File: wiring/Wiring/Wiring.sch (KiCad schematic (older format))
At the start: 4 parts

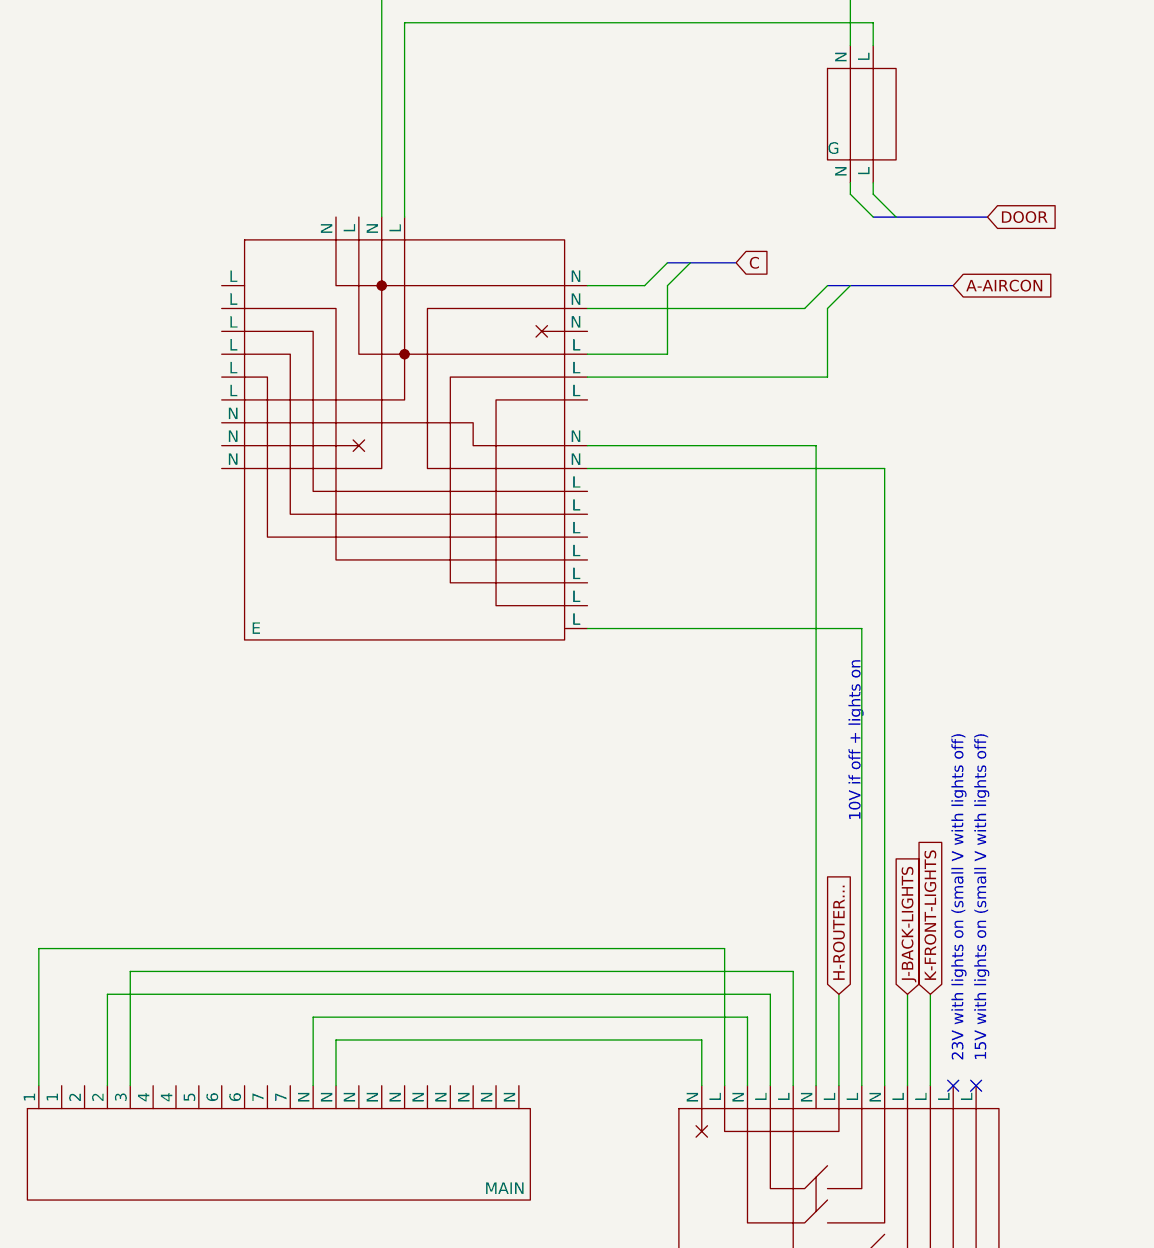
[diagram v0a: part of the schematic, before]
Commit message: Fix wrong wiring
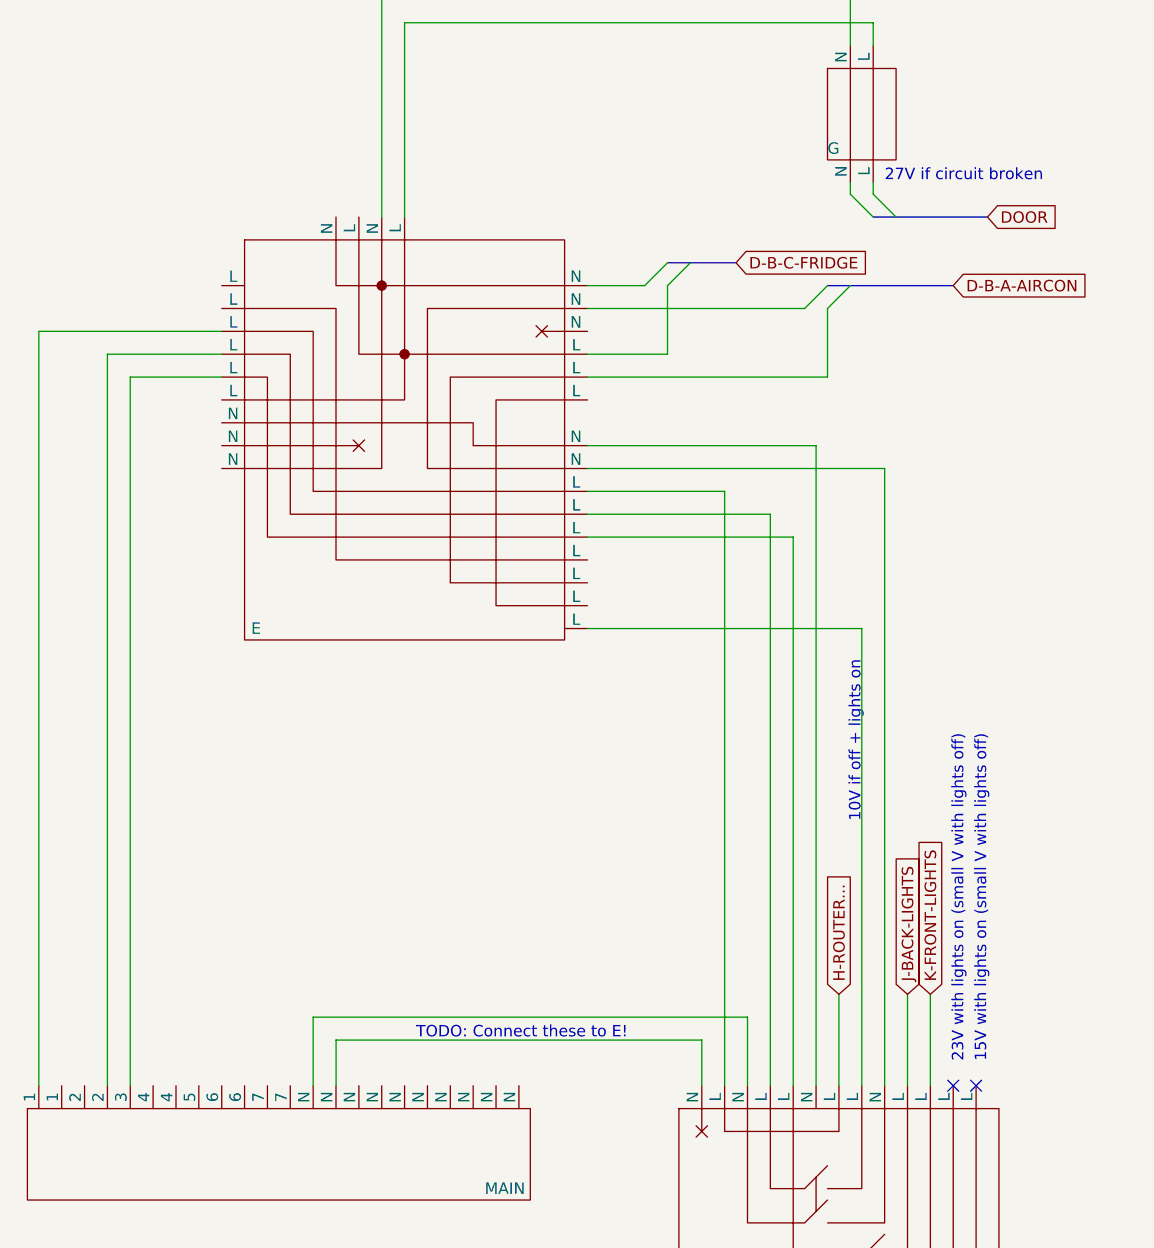
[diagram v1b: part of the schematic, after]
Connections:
- net at U?.2 (L): now also U?.18 (L); no longer U?.1
- net at U?.4 (L): now also U?.19 (L); no longer U?.2
- net at U?.5 (L): now also U?.20 (L); no longer U?.3
- net at U?.5 (L): now also U?.3
- net at U?.6 (L): now also U?.2
- net at U?.7 (L): now also U?.1
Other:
- note added: "27V if circuit broken"
- note added: "TODO: Connect these to E!"
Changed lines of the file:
@@
 	1    0    0    -1
 $EndComp
-Wire Wire Line
-	3900 5400 3900 5000
-Wire Wire Line
-	6800 5000 6800 5400
 Entry Wire Line
 	6950 2000 7050 1900
@@
 	7150 1900 7050 2000
 Text GLabel 7600 1900 2    50   Input ~ 0
-A-AIRCON
+D-B-A-AIRCON
 Entry Wire Line
 	7250 1500 7350 1600
@@
 	6350 2200 6000 2200
 Text GLabel 6650 1800 2    50   Input ~ 0
-C
+D-B-C-FRIDGE
 Wire Wire Line
 	7100 5000 7100 5400
 Text GLabel 7100 5000 1    50   Input ~ 0
 H-ROUTER...
-Wire Wire Line
-	6600 5400 6600 4800
-Wire Wire Line
-	6600 4800 3600 4800
-Wire Wire Line
-	3600 4800 3600 5400
 Text GLabel 7400 5000 1    50   Input ~ 0
 J-BACK-LIGHTS
@@
 	4900 5200 4900 5400
 Wire Wire Line
-	4000 5400 4000 4900
-Wire Wire Line
-	4000 4900 6900 4900
-Wire Wire Line
-	6900 4900 6900 5400
-Wire Wire Line
 	7500 5400 7500 5000
 Text GLabel 7500 5000 1    50   Input ~ 0
@@
 	4800 5100 4800 5400
 Wire Wire Line
-	6800 5000 3900 5000
+	3600 2100 4400 2100
+Wire Wire Line
+	3900 2200 4400 2200
+Wire Wire Line
+	4000 2300 4400 2300
+Wire Wire Line
+	6600 2800 6000 2800
+Wire Wire Line
+	6600 2800 6600 5400
+Wire Wire Line
+	3600 2100 3600 5400
+Wire Wire Line
+	6000 2900 6800 2900
+Wire Wire Line
+	6800 2900 6800 5400
+Wire Wire Line
+	3900 2200 3900 5400
+Wire Wire Line
+	6000 3000 6900 3000
 Wire Bus Line
 	6350 1800 6650 1800
@@
 Wire Bus Line
 	7050 1900 7600 1900
+Wire Wire Line
+	4000 2300 4000 5400
+Wire Wire Line
+	6900 3000 6900 5400
+Text Notes 5250 5200 0    50   ~ 0
+TODO: Connect these to E!
+Text Notes 7300 1450 0    50   ~ 0
+27V if circuit broken
 $EndSCHEMATC

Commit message: Add layout
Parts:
- U1, U2, U3, U4: renamed from U?; footprint (none) -> Package_DFN_QFN:DFN-8-1EP_4x4mm_P0.8mm_EP2.5x3.6mm
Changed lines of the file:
@@
 $EndDescr
 $Comp
-L Wiring:F U?
+L Wiring:F U3
 U 1 1 5ED38158
 P 7050 5850
-F 0 "U?" H 7678 5929 50  0001 L CNN
+F 0 "U3" H 7678 5929 50  0001 L CNN
 F 1 "F" H 7650 5450 50  0000 L CNN
-F 2 "" H 7000 6000 50  0001 C CNN
+F 2 "Package_DFN_QFN:DFN-8-1EP_4x4mm_P0.8mm_EP2.5x3.6mm" H 7000 6000 50  0001 C CNN
 F 3 "" H 7000 6000 50  0001 C CNN
 	1    7050 5850
@@
 $EndComp
 $Comp
-L Wiring:E U?
+L Wiring:E U2
 U 1 1 5ED38C33
 P 5200 2550
-F 0 "U?" H 4525 3500 50  0001 C CNN
+F 0 "U2" H 4525 3500 50  0001 C CNN
 F 1 "E" H 4550 1700 50  0000 C CNN
-F 2 "" H 5200 2550 50  0001 C CNN
+F 2 "Package_DFN_QFN:DFN-8-1EP_4x4mm_P0.8mm_EP2.5x3.6mm" H 5200 2550 50  0001 C CNN
 F 3 "" H 5200 2550 50  0001 C CNN
 	1    5200 2550
@@
 $EndComp
 $Comp
-L Wiring:G U?
+L Wiring:G U4
 U 1 1 5ED3C88F
 P 7200 1150
-F 0 "U?" H 7378 1196 50  0001 L CNN
+F 0 "U4" H 7378 1196 50  0001 L CNN
 F 1 "G" H 7050 1000 50  0000 L CNN
-F 2 "" H 7200 1150 50  0001 C CNN
+F 2 "Package_DFN_QFN:DFN-8-1EP_4x4mm_P0.8mm_EP2.5x3.6mm" H 7200 1150 50  0001 C CNN
 F 3 "" H 7200 1150 50  0001 C CNN
 	1    7200 1150
@@
 	7250 750  7250 850
 $Comp
-L Wiring:MAIN U?
+L Wiring:MAIN U1
 U 1 1 5ED3FA8D
 P 4650 5700
-F 0 "U?" H 3600 5850 50  0001 L CNN
+F 0 "U1" H 3600 5850 50  0001 L CNN
 F 1 "MAIN" H 5550 5550 50  0000 L CNN
-F 2 "" H 4650 6000 50  0001 C CNN
+F 2 "Package_DFN_QFN:DFN-8-1EP_4x4mm_P0.8mm_EP2.5x3.6mm" H 4650 6000 50  0001 C CNN
 F 3 "" H 4650 6000 50  0001 C CNN
 	1    4650 5700

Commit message: Add rough outlines of boxes H, I, J
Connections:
- net H-ROUTER...: no longer names the net of U3.7 (L)
- net J-BACK-LIGHTS: no longer names the net of U3.10 (L)
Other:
- note added: "H"
- note added: "I"
- note added: "J"
- note added: "L"
- note added: "N"
- note added: "Route these through E\n(can't be connected \nstraight to H)"
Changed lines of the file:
@@
 D-B-C-FRIDGE
-Wire Wire Line
-	7100 5000 7100 5400
-Text GLabel 7100 5000 1    50   Input ~ 0
-H-ROUTER...
-Text GLabel 7400 5000 1    50   Input ~ 0
-J-BACK-LIGHTS
-Wire Wire Line
-	7400 5000 7400 5400
 Wire Wire Line
 	6700 5400 6700 5100
@@
 Wire Wire Line
 	6000 3000 6900 3000
-Wire Bus Line
-	6350 1800 6650 1800
-Wire Bus Line
-	7250 1600 7750 1600
-Wire Bus Line
-	7050 1900 7600 1900
 Wire Wire Line
 	4000 2300 4000 5400
@@
 Text Notes 7300 1450 0    50   ~ 0
 27V if circuit broken
+Wire Notes Line
+	9000 2500 9500 2500
+Wire Notes Line
+	9500 2500 9500 3100
+Wire Notes Line
+	9000 3100 9000 2500
+Text Notes 9400 3050 0    50   ~ 0
+H
+Wire Notes Line
+	10500 2500 11000 2500
+Wire Notes Line
+	11000 2500 11000 3100
+Wire Notes Line
+	11000 3100 10500 3100
+Wire Notes Line
+	10500 3100 10500 2500
+Text Notes 10950 3050 0    50   ~ 0
+J
+Wire Wire Line
+	7100 2600 7100 5400
+Text GLabel 11750 2500 2    50   Input ~ 0
+Router
+Entry Wire Line
+	11300 2600 11400 2500
+Wire Wire Line
+	11300 2600 7100 2600
+Wire Wire Line
+	5000 5400 5000 5300
+Wire Wire Line
+	5000 5300 6100 5300
+Wire Wire Line
+	6100 5300 6100 6450
+Wire Wire Line
+	6100 6450 8750 6450
+Wire Wire Line
+	8750 6450 8750 2750
+Entry Wire Line
+	11550 2500 11450 2600
+Wire Wire Line
+	11450 2700 11450 2600
+Wire Notes Line
+	8500 3500 9000 3500
+Wire Notes Line
+	9000 3500 9000 4000
+Wire Notes Line
+	9000 4000 8500 4000
+Wire Notes Line
+	8500 4000 8500 3500
+Text Notes 8950 3950 0    50   ~ 0
+I
+Wire Wire Line
+	7400 2900 11300 2900
+Wire Wire Line
+	7400 2900 7400 5400
+Wire Notes Line
+	9500 3100 9000 3100
+Text Notes 7650 2850 0    50   ~ 0
+Route these through E\n(can't be connected \nstraight to H)
+Wire Wire Line
+	10750 2700 11450 2700
+Wire Wire Line
+	10750 2750 10750 2700
+Wire Wire Line
+	8750 2750 10750 2750
+Wire Wire Line
+	10750 2750 10750 2800
+Wire Wire Line
+	10750 2800 11450 2800
+Connection ~ 10750 2750
+Text Notes 11000 2600 0    50   ~ 0
+L
+Text Notes 11000 2700 0    50   ~ 0
+N
+Text Notes 11000 2800 0    50   ~ 0
+N
+Text Notes 11000 2900 0    50   ~ 0
+L
+Text Notes 10450 2600 0    50   ~ 0
+L
+Text Notes 10450 2750 0    50   ~ 0
+N
+Text Notes 10450 2900 0    50   ~ 0
+L
+Text Notes 9500 2600 0    50   ~ 0
+L
+Text Notes 9500 2900 0    50   ~ 0
+L
+Text Notes 9500 2750 0    50   ~ 0
+N
+Text Notes 8950 2750 0    50   ~ 0
+N
+Text Notes 8950 2600 0    50   ~ 0
+L
+Text Notes 8950 2900 0    50   ~ 0
+L
+Text Notes 8750 3500 0    50   ~ 0
+N
+Text Notes 8750 4100 0    50   ~ 0
+N
+Text GLabel 11750 3000 2    50   Input ~ 0
+BACK-LIGHTS
+Entry Wire Line
+	11300 2900 11400 3000
+Entry Wire Line
+	11450 2900 11550 3000
+Wire Wire Line
+	11450 2800 11450 2900
+Wire Bus Line
+	11400 3000 11750 3000
+Wire Bus Line
+	11400 2500 11750 2500
+Wire Bus Line
+	6350 1800 6650 1800
+Wire Bus Line
+	7250 1600 7750 1600
+Wire Bus Line
+	7050 1900 7600 1900
 $EndSCHEMATC

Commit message: Connect soldering area, fix routing (incomplete)
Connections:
- net at U3.1 (N): now also U2.16 (N); no longer U1.~ (N)
- net at U3.10 (L): now also U2.19 (L)
- net at U3.4 (L): now also U1.~ (N); no longer U2.19 (L)
- net at U3.6 (N): no longer U2.16 (N)
- net at U3.7 (L): now also U2.23 (L)
- net at U2.1 (N): now also U1.~ (N)
- net at U2.2 (N): now also U1.~ (N)
- net at U2.3 (N): now also U1.~ (N)
- net at U2.4 (L): now also U1.~ (N)
- net at U2.6 (L): no longer U1.2
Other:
- note added: "Q"
- note added: "Route more\nwires through\nI! (WIP comp.)"
- note removed: "Route these through E\n(can't be connected \nstraight to H)"
- note removed: "TODO: Connect these to E!"

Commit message: Add B
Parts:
- added U?: B, symbol Wiring:B
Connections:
- net at U2.10 (N): now also U?.10 (N)
- net at U2.11 (N): now also U?.10 (N)
- net at U2.13 (L): now also U?.12 (L)
- net at U2.14 (L): now also U?.12 (L)
- no-connect marks 2 -> 3
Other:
- note added: "D"

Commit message: Add D
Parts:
- added U?: D, symbol Wiring:D
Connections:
- net at U2.10 (N): now also U?.10 (N); no longer U?.10 (N)
- net at U2.11 (N): now also U?.10 (N); no longer U?.10 (N)
- net at U2.13 (L): now also U?.12 (L); no longer U?.12 (L)
- net at U2.14 (L): now also U?.12 (L)
- net at U?.12 (L): now also U?.9 (L); no longer U2.14 (L)
- net at U?.10 (N): now also U?.8 (N)
- new net: U?.10 (N), U?.8 (N) (x2)
- new net: U?.12 (L), U?.9 (L) (x2)
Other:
- note removed: "D"
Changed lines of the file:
@@
 Entry Wire Line
 	12000 700  11900 800
-Wire Wire Line
-	13400 5200 11500 5200
 Text GLabel 12200 700  2    50   Input ~ 0
 C-FRIDGE...
@@
 Wire Wire Line
 	12800 5700 12800 8400
-Wire Wire Line
-	11500 5300 13200 5300
 Wire Wire Line
 	13000 8400 13000 8000
@@
 Wire Wire Line
 	16950 5800 16950 5900
-$Comp
-L Wiring:E U2
-U 1 1 5ED38C33
-P 10700 5550
-F 0 "U2" H 10025 6500 50  0001 C CNN
-F 1 "E" H 10050 4700 50  0000 C CNN
-F 2 "Package_DFN_QFN:DFN-8-1EP_4x4mm_P0.8mm_EP2.5x3.6mm" H 10700 5550 50  0001 C CNN
-F 3 "" H 10700 5550 50  0001 C CNN
-	1    10700 5550
-	1    0    0    -1
-$EndComp
 Wire Wire Line
 	12300 8400 12300 8000
@@
 Wire Wire Line
 	10950 3650 10600 3650
-Wire Notes Line
-	13000 3500 13500 3500
-Wire Notes Line
-	13500 3500 13500 4000
-Wire Notes Line
-	13500 4000 13000 4000
-Wire Notes Line
-	13000 4000 13000 3500
-Text Notes 13450 4000 0    50   ~ 0
-D
 Wire Wire Line
 	11500 1950 11600 1950
@@
 	11400 1950 11300 1850
 Wire Wire Line
-	13100 5000 13100 1800
-Wire Wire Line
-	13100 1800 12800 1800
-Wire Wire Line
-	11500 5000 13100 5000
-Wire Wire Line
-	13200 1700 12800 1700
-Wire Wire Line
-	13200 1700 13200 5300
-Wire Wire Line
 	11900 800  11900 1100
 Wire Wire Line
 	11800 1100 11800 800
-Wire Wire Line
-	13300 4900 13300 1600
-Wire Wire Line
-	13300 1600 12800 1600
-Wire Wire Line
-	11500 4900 13300 4900
-Wire Wire Line
-	12800 1500 13400 1500
-Wire Wire Line
-	13400 1500 13400 5200
+$Comp
+L Wiring:D U?
+U 1 1 5EE0B04E
+P 14200 1550
+F 0 "U?" H 13650 2050 50  0001 C CNN
+F 1 "D" H 14728 1467 50  0000 L CNN
+F 2 "" H 13500 2050 50  0001 C CNN
+F 3 "" H 13500 2050 50  0001 C CNN
+	1    14200 1550
+	1    0    0    -1
+$EndComp
+Wire Wire Line
+	13950 2150 13950 5000
+Wire Wire Line
+	11500 5000 13950 5000
+Wire Wire Line
+	12800 1800 13600 1800
+Wire Wire Line
+	14050 2150 14050 5300
+Wire Wire Line
+	12800 1700 13600 1700
+Wire Wire Line
+	11500 5300 14050 5300
+Wire Wire Line
+	14150 2150 14150 4900
+Wire Wire Line
+	11500 4900 14150 4900
+Wire Wire Line
+	12800 1600 13600 1600
+Wire Wire Line
+	14250 2150 14250 5200
+Wire Wire Line
+	12800 1500 13600 1500
+Wire Wire Line
+	11500 5200 14250 5200
+Wire Wire Line
+	12800 1300 13600 1300
+Wire Wire Line
+	12800 1400 13600 1400
 Wire Bus Line
 	10850 1850 11400 1850
 Wire Bus Line
+	12600 900  12850 900
+Wire Bus Line
 	11600 2950 11900 2950
 Wire Bus Line
@@
 Wire Bus Line
 	11050 4600 11550 4600
-Wire Bus Line
-	12600 900  12850 900
+$Comp
+L Wiring:E U2
+U 1 1 5ED38C33
+P 10700 5550
+F 0 "U2" H 10025 6500 50  0001 C CNN
+F 1 "E" H 10050 4700 50  0000 C CNN
+F 2 "Package_DFN_QFN:DFN-8-1EP_4x4mm_P0.8mm_EP2.5x3.6mm" H 10700 5550 50  0001 C CNN
+F 3 "" H 10700 5550 50  0001 C CNN
+	1    10700 5550
+	1    0    0    -1
+$EndComp
 $EndSCHEMATC
